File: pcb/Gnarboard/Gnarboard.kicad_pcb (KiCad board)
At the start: 2 copper layers, 184 x 136 mm, 138 parts, among them J1 N2K, J10 Screw_Terminal_01x02, J11 Screw_Terminal_01x02, J12 Screw_Terminal_01x02, J2 I2C, J3 Screw_Terminal_01x09, J5 Screw_Terminal_01x02, J6 Screw_Terminal_01x02, J7 Screw_Terminal_01x02, J8 Screw_Terminal_01x02, J9 Screw_Terminal_01x02, Q1 BC817, Q10 IRF4905, Q11 BC817, Q12 IRF4905, Q13 BC817, Q14 IRF4905, Q15 BC817, Q16 IRF4905, Q2 IRF4905, Q3 BC817, Q4 IRF4905, Q5 BC817, Q6 IRF4905, Q7 BC817, Q8 IRF4905, Q9 BC817, U1 ESP32-DEVKITC, U10 ACS725xLCTR-20AU, U11 ACS725xLCTR-20AU, U12 ACS725xLCTR-20AU, U2 MCP3208, U3 R-78B3.3-2.0, U5 ACS725xLCTR-20AU, U6 ACS725xLCTR-20AU, U7 ACS725xLCTR-20AU, U8 ACS725xLCTR-20AU, U9 ACS725xLCTR-20AU

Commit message: added in mounting holes.
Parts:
- added REF**: MountingHole_2.5mm_Pad_TopOnly, MountingHole:MountingHole_2.5mm_Pad_TopOnly, F.Cu at (3.00, 133.0)
- added REF**: MountingHole_2.5mm_Pad_TopOnly, MountingHole:MountingHole_2.5mm_Pad_TopOnly, F.Cu at (181.2, 84.5)
- added REF**: MountingHole_2.5mm_Pad_TopOnly, MountingHole:MountingHole_2.5mm_Pad_TopOnly, F.Cu at (181.2, 23.0)
- added REF**: MountingHole_2.5mm_Pad_TopOnly, MountingHole:MountingHole_2.5mm_Pad_TopOnly, F.Cu at (3.00, 3.00)
- moved C6 65.9 mm to (65.8, 95.3)
- moved C7 65.9 mm to (65.8, 90.4)
- moved C8 65.9 mm to (65.8, 92.8)
- moved D20 65.9 mm to (77.9, 67.6)
- moved D21 65.9 mm to (97.0, 67.6)
- moved D22 65.9 mm to (116.0, 67.6)
- moved J11 65.9 mm to (154.2, 108.6)
- moved J8 65.9 mm to (97.0, 108.6)
- moved J9 65.9 mm to (116.1, 108.6)
- moved Q10 65.9 mm to (115.1, 80.6)
- moved Q14 65.9 mm to (153.2, 80.6)
- moved Q8 65.9 mm to (96.0, 80.6)
- moved C1 65.9 mm to (28.0, 5.60)
- moved C10 65.9 mm to (84.9, 90.4)
- moved C11 65.9 mm to (84.9, 92.8)
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
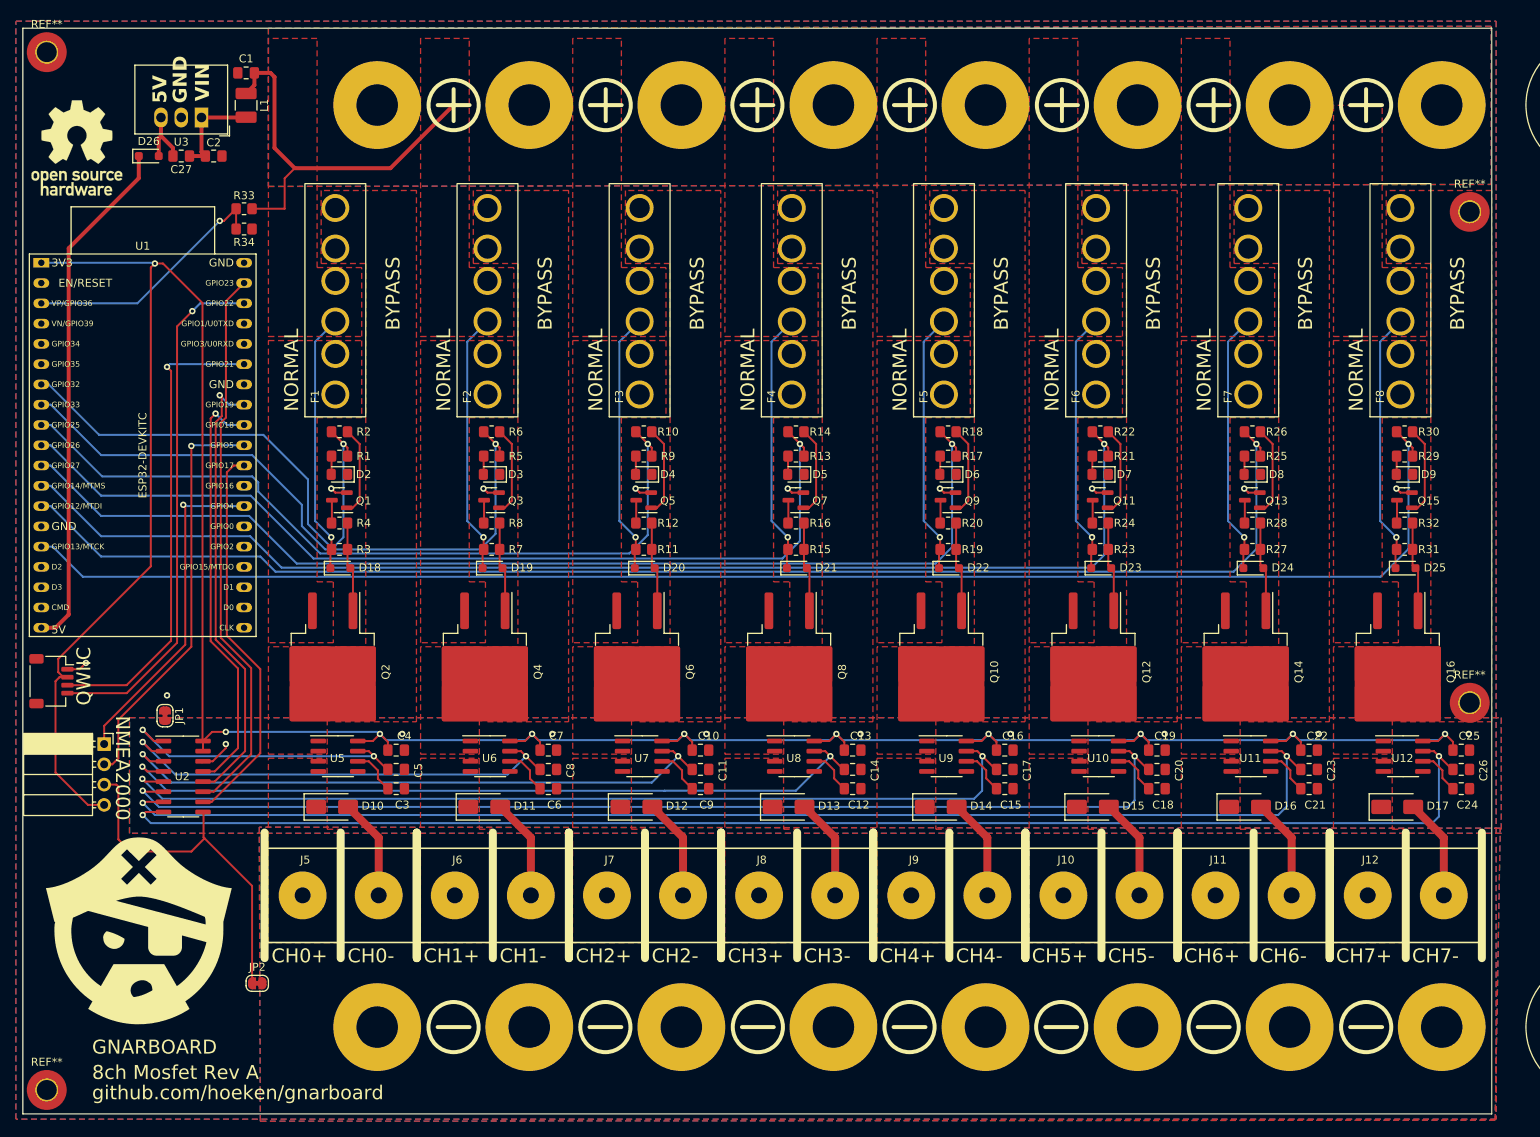
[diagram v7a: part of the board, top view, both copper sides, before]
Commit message: okay fixed drcs.  think its good to go.
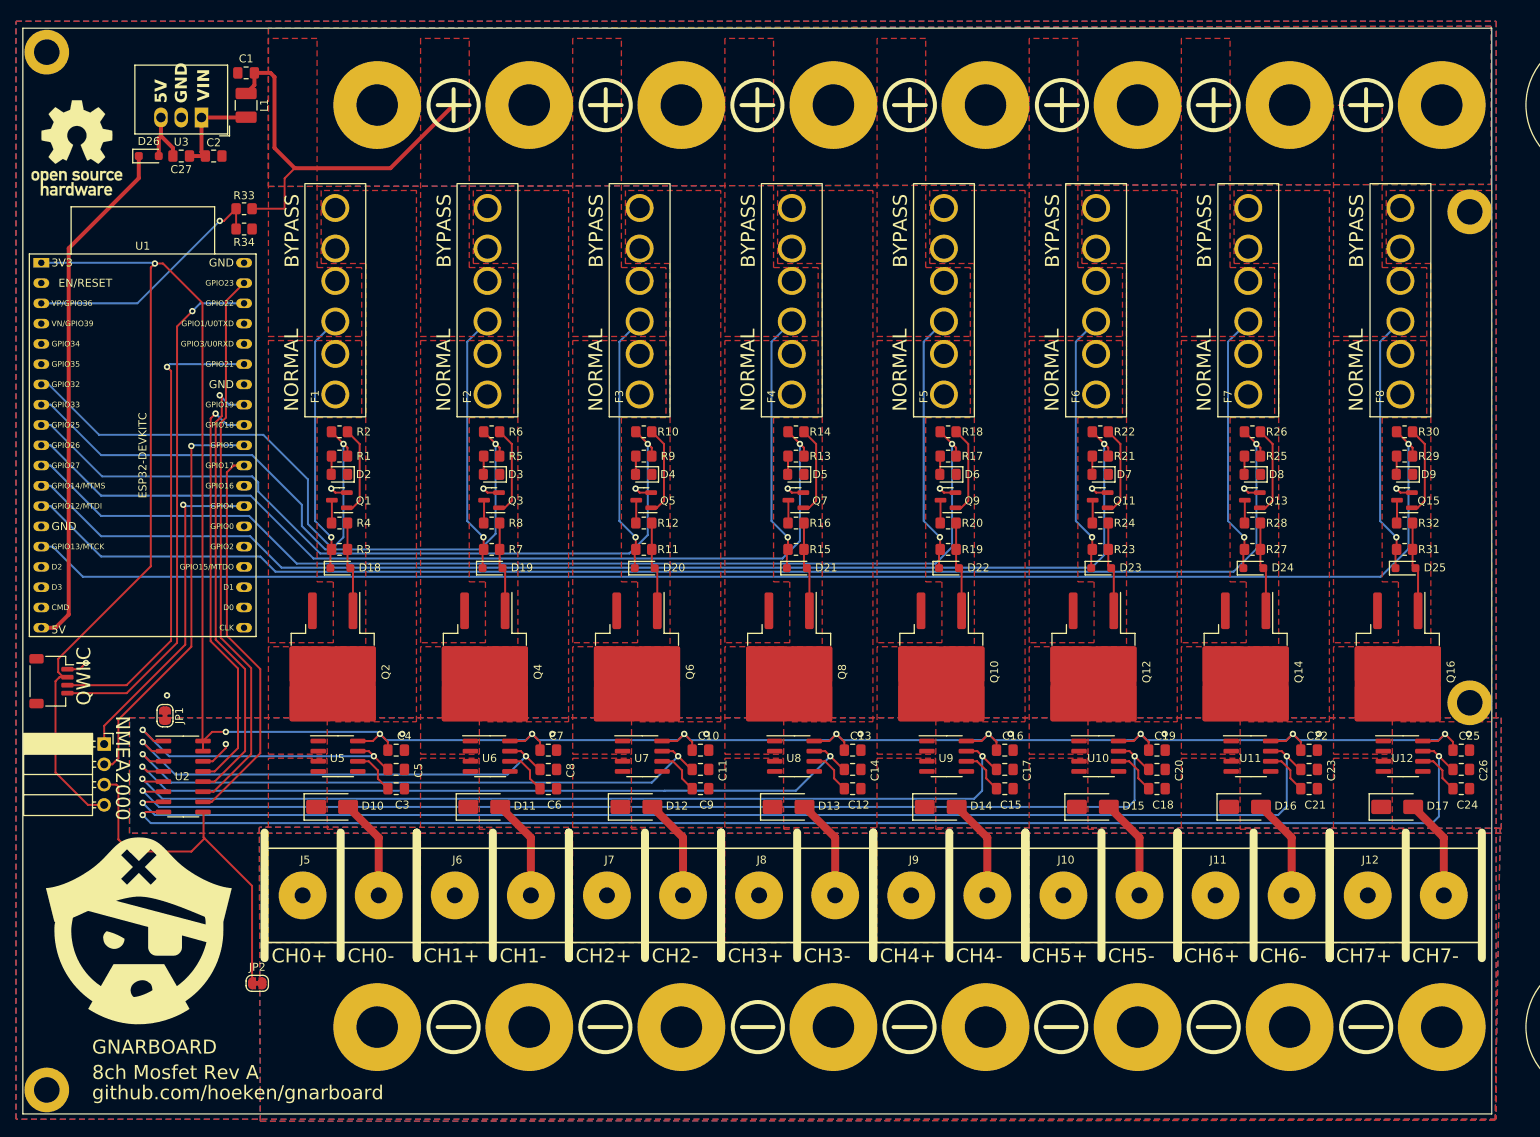
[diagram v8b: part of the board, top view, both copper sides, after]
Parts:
- REF** (x4): value MountingHole_2.5mm_Pad_TopOnly -> MountingHole_3.2mm_M3_DIN965_Pad; footprint MountingHole:MountingHole_2.5mm_Pad_TopOnly -> MountingHole:MountingHole_3.2mm_M3_DIN965_Pad
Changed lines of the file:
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@@
     )
     (pad_to_mask_clearance 0)
-    (aux_axis_origin 61.184 160.376)
+    (aux_axis_origin 0 136)
     (pcbplotparams
       (layerselection 0x0000000_7ffffffe)
@@
     )
   )
-  (footprint "MountingHole:MountingHole_2.5mm_Pad_TopOnly" (layer "F.Cu")
+  (footprint "MountingHole:MountingHole_3.2mm_M3_DIN965_Pad" (layer "F.Cu")
     (at 3 133)
-    (descr "Mounting Hole 2.5mm")
-    (tags "mounting hole 2.5mm")
+    (descr "Mounting Hole 3.2mm, M3, DIN965")
+    (tags "mounting hole 3.2mm m3 din965")
     (attr exclude_from_pos_files exclude_from_bom)
-    (fp_text reference "REF**" (at 0 -3.5) (layer "F.SilkS")
+    (fp_text reference "REF**" (at 0 -3.8) (layer "F.SilkS") hide
         (effects (font (size 1 1) (thickness 0.15)))
     )
-    (fp_text value "MountingHole_2.5mm_Pad_TopOnly" (at 0 3.5) (layer "F.Fab")
+    (fp_text value "MountingHole_3.2mm_M3_DIN965_Pad" (at 0 3.8) (layer "F.Fab")
         (effects (font (size 1 1) (thickness 0.15)))
     )
@@
         (effects (font (size 1 1) (thickness 0.15)))
     )
-    (fp_circle (center 0 0) (end 2.5 0)
+    (fp_circle (center 0 0) (end 2.8 0)
       (stroke (width 0.15) (type solid)) (fill none) (layer "Cmts.User"))
-    (fp_circle (center 0 0) (end 2.75 0)
+    (fp_circle (center 0 0) (end 3.05 0)
       (stroke (width 0.05) (type solid)) (fill none) (layer "F.CrtYd"))
-    (pad "1" thru_hole circle (at 0 0) (size 2.9 2.9) (drill 2.5) (layers "*.Cu" "*.Mask"))
-    (pad "1" connect circle (at 0 0) (size 5 5) (layers "F.Cu" "F.Mask"))
+    (pad "1" thru_hole circle (at 0 0) (size 5.6 5.6) (drill 3.2) (layers "*.Cu" "*.Mask"))
   )
   (footprint "Resistor_SMD:R_0805_2012Metric_Pad1.20x1.40mm_HandSolder" (layer "F.Cu")
@@
       (stroke (width 0.01) (type solid)) (fill solid) (layer "F.SilkS"))
   )
-  (footprint "MountingHole:MountingHole_2.5mm_Pad_TopOnly" (layer "F.Cu")
+  (footprint "MountingHole:MountingHole_3.2mm_M3_DIN965_Pad" (layer "F.Cu")
     (at 181.25 84.5)
-    (descr "Mounting Hole 2.5mm")
-    (tags "mounting hole 2.5mm")
+    (descr "Mounting Hole 3.2mm, M3, DIN965")
+    (tags "mounting hole 3.2mm m3 din965")
     (attr exclude_from_pos_files exclude_from_bom)
-    (fp_text reference "REF**" (at 0 -3.5) (layer "F.SilkS")
+    (fp_text reference "REF**" (at 0 -3.8) (layer "F.SilkS") hide
         (effects (font (size 1 1) (thickness 0.15)))
     )
-    (fp_text value "MountingHole_2.5mm_Pad_TopOnly" (at 0 3.5) (layer "F.Fab")
+    (fp_text value "MountingHole_3.2mm_M3_DIN965_Pad" (at 0 3.8) (layer "F.Fab")
         (effects (font (size 1 1) (thickness 0.15)))
     )
@@
         (effects (font (size 1 1) (thickness 0.15)))
     )
-    (fp_circle (center 0 0) (end 2.5 0)
+    (fp_circle (center 0 0) (end 2.8 0)
       (stroke (width 0.15) (type solid)) (fill none) (layer "Cmts.User"))
-    (fp_circle (center 0 0) (end 2.75 0)
+    (fp_circle (center 0 0) (end 3.05 0)
       (stroke (width 0.05) (type solid)) (fill none) (layer "F.CrtYd"))
-    (pad "1" thru_hole circle (at 0 0) (size 2.9 2.9) (drill 2.5) (layers "*.Cu" "*.Mask"))
-    (pad "1" connect circle (at 0 0) (size 5 5) (layers "F.Cu" "F.Mask"))
+    (pad "1" thru_hole circle (at 0 0) (size 5.6 5.6) (drill 3.2) (layers "*.Cu" "*.Mask"))
   )
   (footprint "LED_SMD:LED_0805_2012Metric_Pad1.15x1.40mm_HandSolder" (layer "F.Cu")
@@
     )
   )
-  (footprint "MountingHole:MountingHole_2.5mm_Pad_TopOnly" (layer "F.Cu")
+  (footprint "MountingHole:MountingHole_3.2mm_M3_DIN965_Pad" (layer "F.Cu")
     (at 181.25 23)
-    (descr "Mounting Hole 2.5mm")
-    (tags "mounting hole 2.5mm")
+    (descr "Mounting Hole 3.2mm, M3, DIN965")
+    (tags "mounting hole 3.2mm m3 din965")
     (attr exclude_from_pos_files exclude_from_bom)
-    (fp_text reference "REF**" (at 0 -3.5) (layer "F.SilkS")
+    (fp_text reference "REF**" (at 0 -3.8) (layer "F.SilkS") hide
         (effects (font (size 1 1) (thickness 0.15)))
     )
-    (fp_text value "MountingHole_2.5mm_Pad_TopOnly" (at 0 3.5) (layer "F.Fab")
+    (fp_text value "MountingHole_3.2mm_M3_DIN965_Pad" (at 0 3.8) (layer "F.Fab")
         (effects (font (size 1 1) (thickness 0.15)))
     )
@@
         (effects (font (size 1 1) (thickness 0.15)))
     )
-    (fp_circle (center 0 0) (end 2.5 0)
+    (fp_circle (center 0 0) (end 2.8 0)
       (stroke (width 0.15) (type solid)) (fill none) (layer "Cmts.User"))
-    (fp_circle (center 0 0) (end 2.75 0)
+    (fp_circle (center 0 0) (end 3.05 0)
       (stroke (width 0.05) (type solid)) (fill none) (layer "F.CrtYd"))
-    (pad "1" thru_hole circle (at 0 0) (size 2.9 2.9) (drill 2.5) (layers "*.Cu" "*.Mask"))
-    (pad "1" connect circle (at 0 0) (size 5 5) (layers "F.Cu" "F.Mask"))
+    (pad "1" thru_hole circle (at 0 0) (size 5.6 5.6) (drill 3.2) (layers "*.Cu" "*.Mask"))
   )
   (footprint "Capacitor_SMD:C_0805_2012Metric_Pad1.18x1.45mm_HandSolder" (layer "F.Cu")
@@
     )
   )
-  (footprint "MountingHole:MountingHole_2.5mm_Pad_TopOnly" (layer "F.Cu")
+  (footprint "MountingHole:MountingHole_3.2mm_M3_DIN965_Pad" (layer "F.Cu")
     (at 3 3)
-    (descr "Mounting Hole 2.5mm")
-    (tags "mounting hole 2.5mm")
+    (descr "Mounting Hole 3.2mm, M3, DIN965")
+    (tags "mounting hole 3.2mm m3 din965")
     (attr exclude_from_pos_files exclude_from_bom)
-    (fp_text reference "REF**" (at 0 -3.5) (layer "F.SilkS")
+    (fp_text reference "REF**" (at 0 -3.8) (layer "F.SilkS") hide
         (effects (font (size 1 1) (thickness 0.15)))
     )
-    (fp_text value "MountingHole_2.5mm_Pad_TopOnly" (at 0 3.5) (layer "F.Fab")
+    (fp_text value "MountingHole_3.2mm_M3_DIN965_Pad" (at 0 3.8) (layer "F.Fab")
         (effects (font (size 1 1) (thickness 0.15)))
     )
@@
         (effects (font (size 1 1) (thickness 0.15)))
     )
-    (fp_circle (center 0 0) (end 2.5 0)
+    (fp_circle (center 0 0) (end 2.8 0)
       (stroke (width 0.15) (type solid)) (fill none) (layer "Cmts.User"))
-    (fp_circle (center 0 0) (end 2.75 0)
+    (fp_circle (center 0 0) (end 3.05 0)
       (stroke (width 0.05) (type solid)) (fill none) (layer "F.CrtYd"))
-    (pad "1" thru_hole circle (at 0 0) (size 2.9 2.9) (drill 2.5) (layers "*.Cu" "*.Mask"))
-    (pad "1" connect circle (at 0 0) (size 5 5) (layers "F.Cu" "F.Mask"))
+    (pad "1" thru_hole circle (at 0 0) (size 5.6 5.6) (drill 3.2) (layers "*.Cu" "*.Mask"))
   )
   (footprint "Resistor_SMD:R_0805_2012Metric_Pad1.20x1.40mm_HandSolder" (layer "F.Cu")
@@
   )
   (gr_text "VIN" (at 23.525 9.152 90) (layer "F.SilkS")
-    (effects (font (size 1.75 1.75) (thickness 0.3) bold) (justify left bottom))
+    (effects (font (size 1.5 1.5) (thickness 0.3) bold) (justify left bottom))
   )
   (gr_text "CH3+" (at 88.291 117.229) (layer "F.SilkS")
     (effects (font (size 1.75 1.75) (thickness 0.2)) (justify left bottom))
   )
-  (gr_text "BYPASS" (at 66.451 37.854 90) (layer "F.SilkS")
+  (gr_text "BYPASS" (at 53.8 30 90) (layer "F.SilkS")
     (effects (font (size 1.75 1.75) (thickness 0.3)) (justify left bottom))
   )
@@
     (effects (font (size 1.75 1.75) (thickness 0.3)) (justify left bottom))
   )
-  (gr_text "BYPASS" (at 47.401 37.854 90) (layer "F.SilkS")
+  (gr_text "BYPASS" (at 34.75 30 90) (layer "F.SilkS")
     (effects (font (size 1.75 1.75) (thickness 0.3)) (justify left bottom))
   )
   (gr_text "5V" (at 18.191 9.406 90) (layer "F.SilkS")
-    (effects (font (size 1.75 1.75) (thickness 0.3) bold) (justify left bottom))
+    (effects (font (size 1.5 1.5) (thickness 0.25) bold) (justify left bottom))
   )
   (gr_text "CH4-" (at 116.866 117.229) (layer "F.SilkS")
     (effects (font (size 1.75 1.75) (thickness 0.2)) (justify left bottom))
   )
-  (gr_text "BYPASS" (at 142.651 37.854 90) (layer "F.SilkS")
+  (gr_text "BYPASS" (at 130 30 90) (layer "F.SilkS")
     (effects (font (size 1.75 1.75) (thickness 0.3)) (justify left bottom))
   )
-  (gr_text "BYPASS" (at 161.701 37.854 90) (layer "F.SilkS")
+  (gr_text "BYPASS" (at 149.05 30 90) (layer "F.SilkS")
     (effects (font (size 1.75 1.75) (thickness 0.3)) (justify left bottom))
   )
@@
     (effects (font (size 1.75 1.75) (thickness 0.2)) (justify left bottom))
   )
-  (gr_text "BYPASS" (at 85.501 37.854 90) (layer "F.SilkS")
+  (gr_text "BYPASS" (at 72.85 30 90) (layer "F.SilkS")
     (effects (font (size 1.75 1.75) (thickness 0.3)) (justify left bottom))
   )
@@
     (effects (font (size 1.75 1.75) (thickness 0.2)) (justify left bottom))
   )
-  (gr_text "BYPASS" (at 104.551 37.854 90) (layer "F.SilkS")
+  (gr_text "BYPASS" (at 91.9 30 90) (layer "F.SilkS")
     (effects (font (size 1.75 1.75) (thickness 0.3)) (justify left bottom))
   )
@@
   )
   (gr_text "GND" (at 20.731 9.406 90) (layer "F.SilkS")
-    (effects (font (size 1.75 1.75) (thickness 0.3) bold) (justify left bottom))
+    (effects (font (size 1.5 1.5) (thickness 0.3) bold) (justify left bottom))
   )
   (gr_text "NORMAL" (at 34.701 48.014 90) (layer "F.SilkS")
@@
     (effects (font (size 1.75 1.75) (thickness 0.3)) (justify left bottom))
   )
-  (gr_text "BYPASS" (at 180.751 37.854 90) (layer "F.SilkS")
+  (gr_text "BYPASS" (at 168.1 30 90) (layer "F.SilkS")
     (effects (font (size 1.75 1.75) (thickness 0.3)) (justify left bottom))
   )
@@
     (effects (font (size 1.75 1.75) (thickness 0.2)) (justify left bottom))
   )
-  (gr_text "BYPASS" (at 123.601 37.854 90) (layer "F.SilkS")
+  (gr_text "BYPASS" (at 110.95 30 90) (layer "F.SilkS")
     (effects (font (size 1.75 1.75) (thickness 0.3)) (justify left bottom))
   )
